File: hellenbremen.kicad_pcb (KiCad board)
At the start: 4 copper layers, 102 x 107 mm, 48 parts, among them J2 Conn_01x03_Pin, J3 USB_C_Receptacle_USB2.0_16P, M1 Module-stlink-0.1, M2 Module-power_12and5V-0.2, M3 Module-mega-mcu144-0.6, M4 Module-vr-max9924-0.1, M5 Module-knock-0.2, M6 Module-knock-0.2, Q1 ISL9V3040D3ST, Q2 ISL9V3040D3ST, U1 RNBD451PE-I100, U2 VNLD5160TR-E, U3 VNLD5160TR-E, U4 VNLD5160TR-E

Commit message: Setting exclude from bom property
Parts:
- renumbered G1 to G***, G2 to G***
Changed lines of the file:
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@@
 		(layer "F.Cu")
 		(at 145.11 130.886)
-		(property "Reference" "G1"
+		(property "Reference" "G***"
 			(at 0 4.14782 0)
 			(layer "F.SilkS")
@@
 			)
 		)
-		(attr through_hole exclude_from_bom)
+		(attr board_only exclude_from_pos_files exclude_from_bom)
 		(fp_poly
 			(pts
@@
 		(layer "F.Cu")
 		(at 155.16 136.386)
-		(property "Reference" "G2"
+		(property "Reference" "G***"
 			(at -5 -6.5 0)
 			(layer "F.SilkS")
@@
 			)
 		)
-		(attr through_hole exclude_from_bom)
+		(attr board_only exclude_from_pos_files exclude_from_bom)
 		(fp_line
 			(start -2.5 -1)

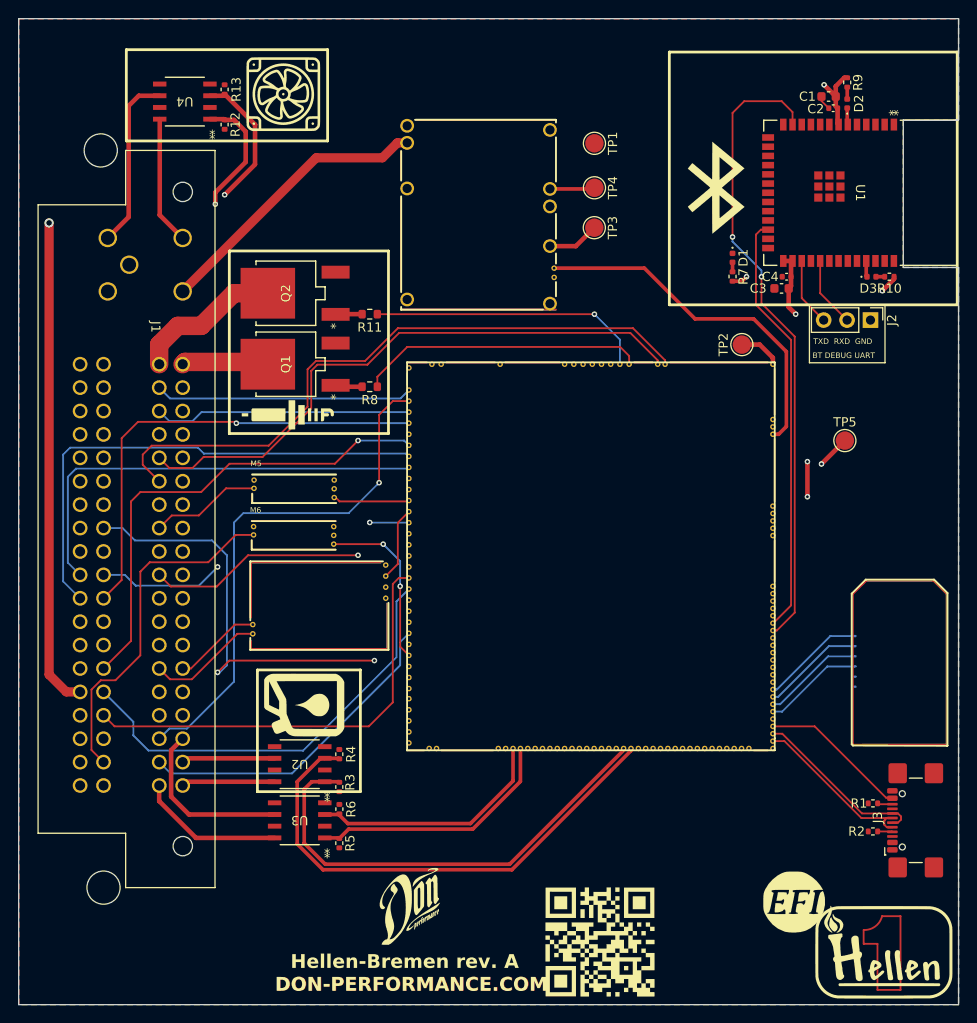
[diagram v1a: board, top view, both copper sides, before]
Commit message: interconnected isolated grounds, minor routing changes
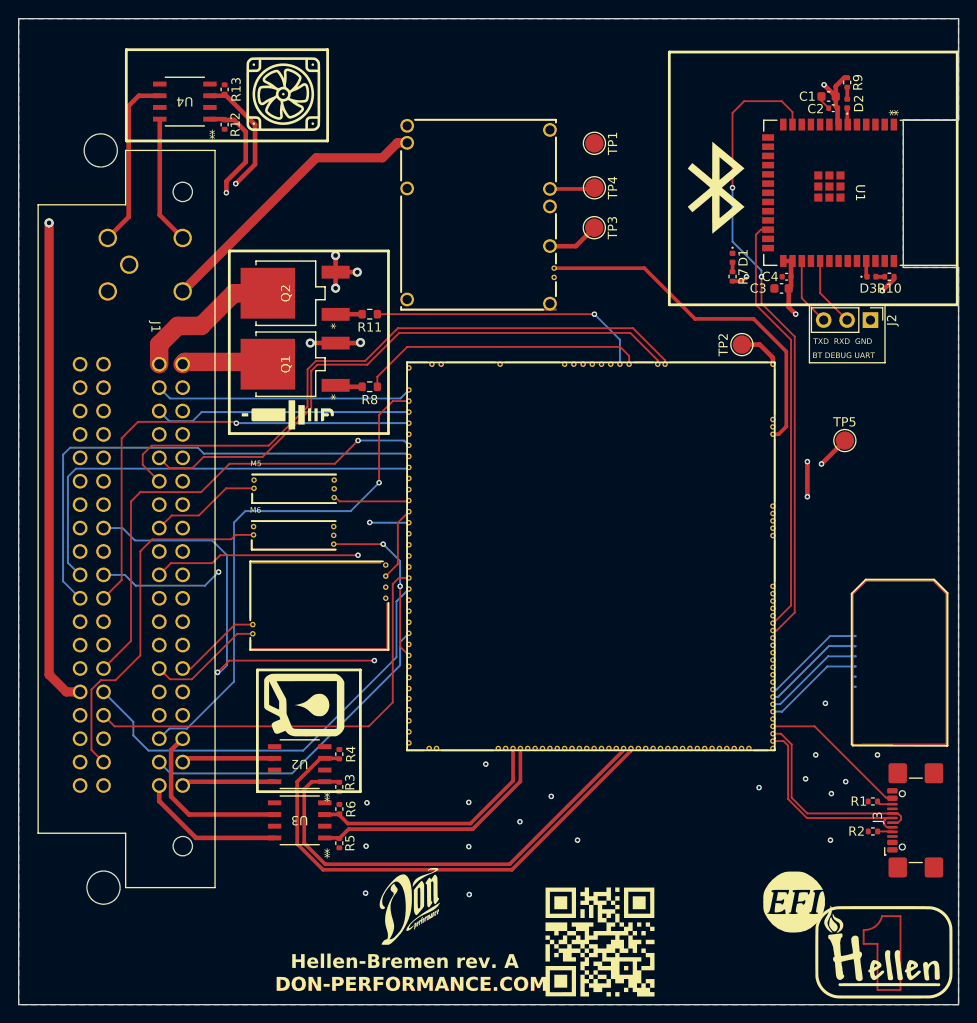
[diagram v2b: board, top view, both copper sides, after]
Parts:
- moved R1 0.21 mm to (153.7, 119.9)
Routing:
- net GND: track 1.60 -> 11.9 mm, vias 0 -> 23
- net Net-(M3-USBM): track 18.3 -> 21.7 mm
- net Net-(M3-USBP): track 19.0 -> 22.4 mm
- net RAW_KNOCK_R: track 38.3 -> 39.6 mm
- net IN_JSS: track 29.6 -> 28.5 mm

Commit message: Fiducial Marks and Via Stitching
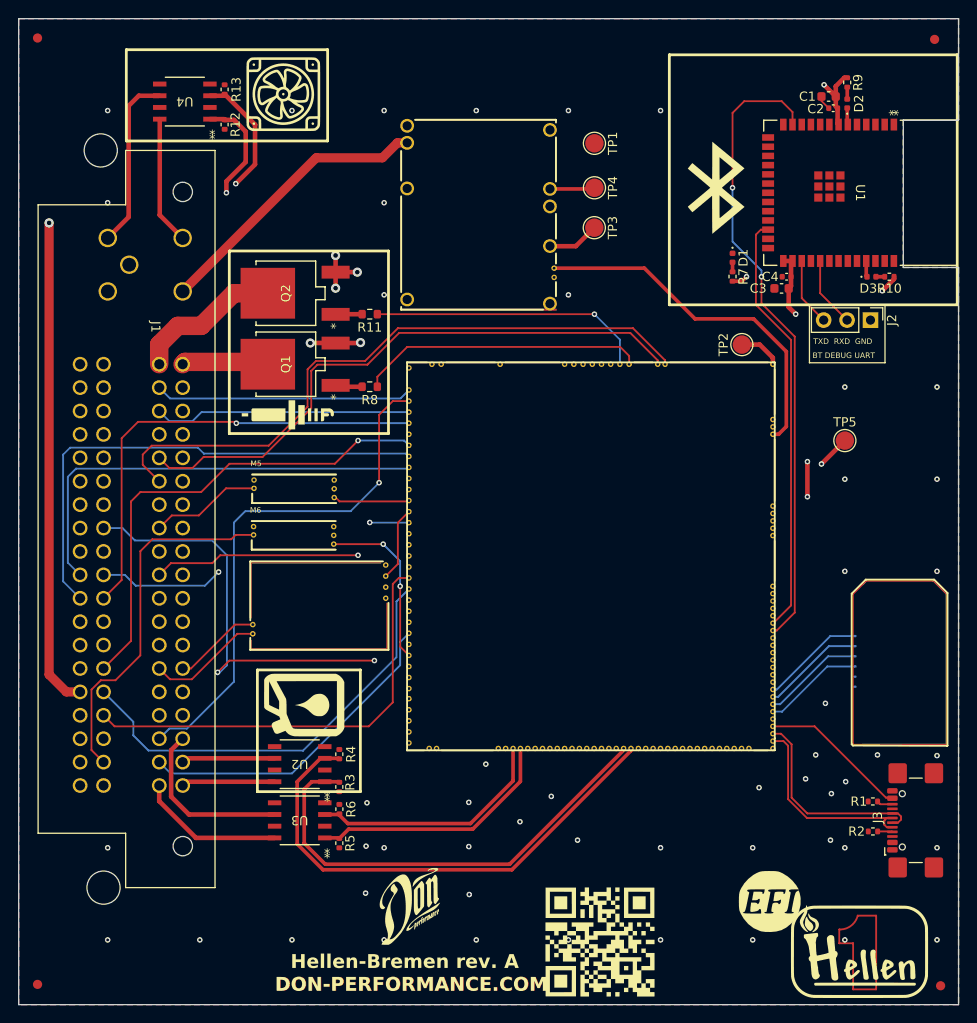
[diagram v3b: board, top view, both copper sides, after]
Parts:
- added FID1: Fiducial, Fiducial:Fiducial_1mm_Mask2mm, F.Cu at (63.0, 37.1)
- added FID2: Fiducial, Fiducial:Fiducial_1mm_Mask2mm, F.Cu at (160.4, 37.2)
- added FID3: Fiducial, Fiducial:Fiducial_1mm_Mask2mm, F.Cu at (63.0, 139.8)
- added FID4: Fiducial, Fiducial:Fiducial_1mm_Mask2mm, F.Cu at (161.0, 139.9)
- moved G*** 2.65 mm to (142.5, 130.8)
- moved G*** 2.65 mm to (152.5, 136.3)
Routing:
- net GND: vias 23 -> 56

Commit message: Fiducial Marks and Via Stitching
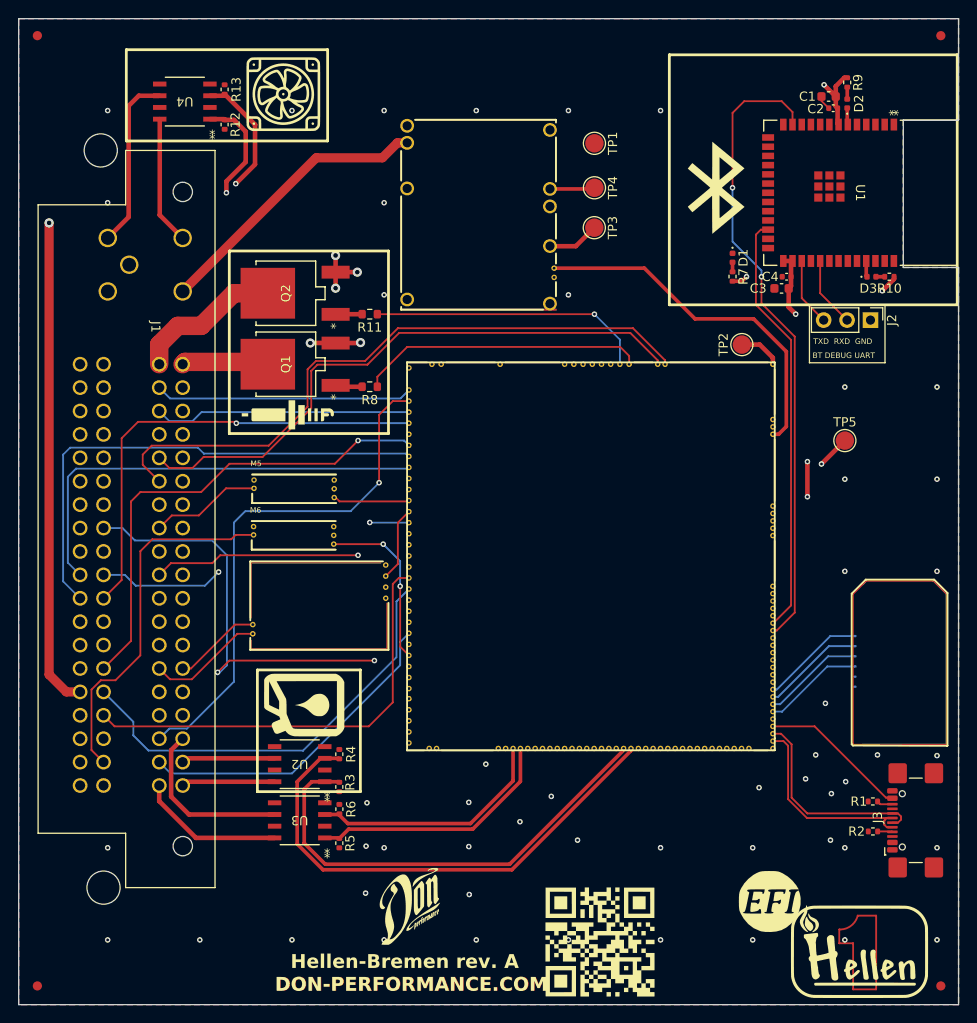
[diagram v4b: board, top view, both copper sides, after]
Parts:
- moved FID2 0.79 mm to (161.0, 36.8)
- moved FID1 0.26 mm to (63.0, 36.8)
- moved FID3 0.17 mm to (63.0, 140.0)
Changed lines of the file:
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@@
 	(footprint "Fiducial:Fiducial_1mm_Mask2mm"
 		(layer "F.Cu")
-		(at 63.01 37.086 -90)
+		(at 62.992 36.83 -90)
 		(descr "Circular Fiducial, 1mm bare copper, 2mm soldermask opening (Level A)")
 		(tags "fiducial")
@@
 	(footprint "Fiducial:Fiducial_1mm_Mask2mm"
 		(layer "F.Cu")
-		(at 161.01 139.936 90)
+		(at 161.036 139.954 90)
 		(descr "Circular Fiducial, 1mm bare copper, 2mm soldermask opening (Level A)")
 		(tags "fiducial")
@@
 	(footprint "Fiducial:Fiducial_1mm_Mask2mm"
 		(layer "F.Cu")
-		(at 63.01 139.786 -90)
+		(at 62.992 139.954 -90)
 		(descr "Circular Fiducial, 1mm bare copper, 2mm soldermask opening (Level A)")
 		(tags "fiducial")
@@
 	(footprint "Fiducial:Fiducial_1mm_Mask2mm"
 		(layer "F.Cu")
-		(at 160.36 37.236 90)
+		(at 161.036 36.83 90)
 		(descr "Circular Fiducial, 1mm bare copper, 2mm soldermask opening (Level A)")
 		(tags "fiducial")
